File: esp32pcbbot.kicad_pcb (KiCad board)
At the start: 2 copper layers, 110 x 170 mm, 44 parts, among them IC1 BMI055, J1 TB002-500-02BE, J2 TB002-500-02BE, J3 TB002-500-02BE, J4 215299-4, J5 SSQ-120-01-L-D, J6 215299-4, Q1 2N7002, Q2 2N7002, Q3 Q_Photo_NPN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

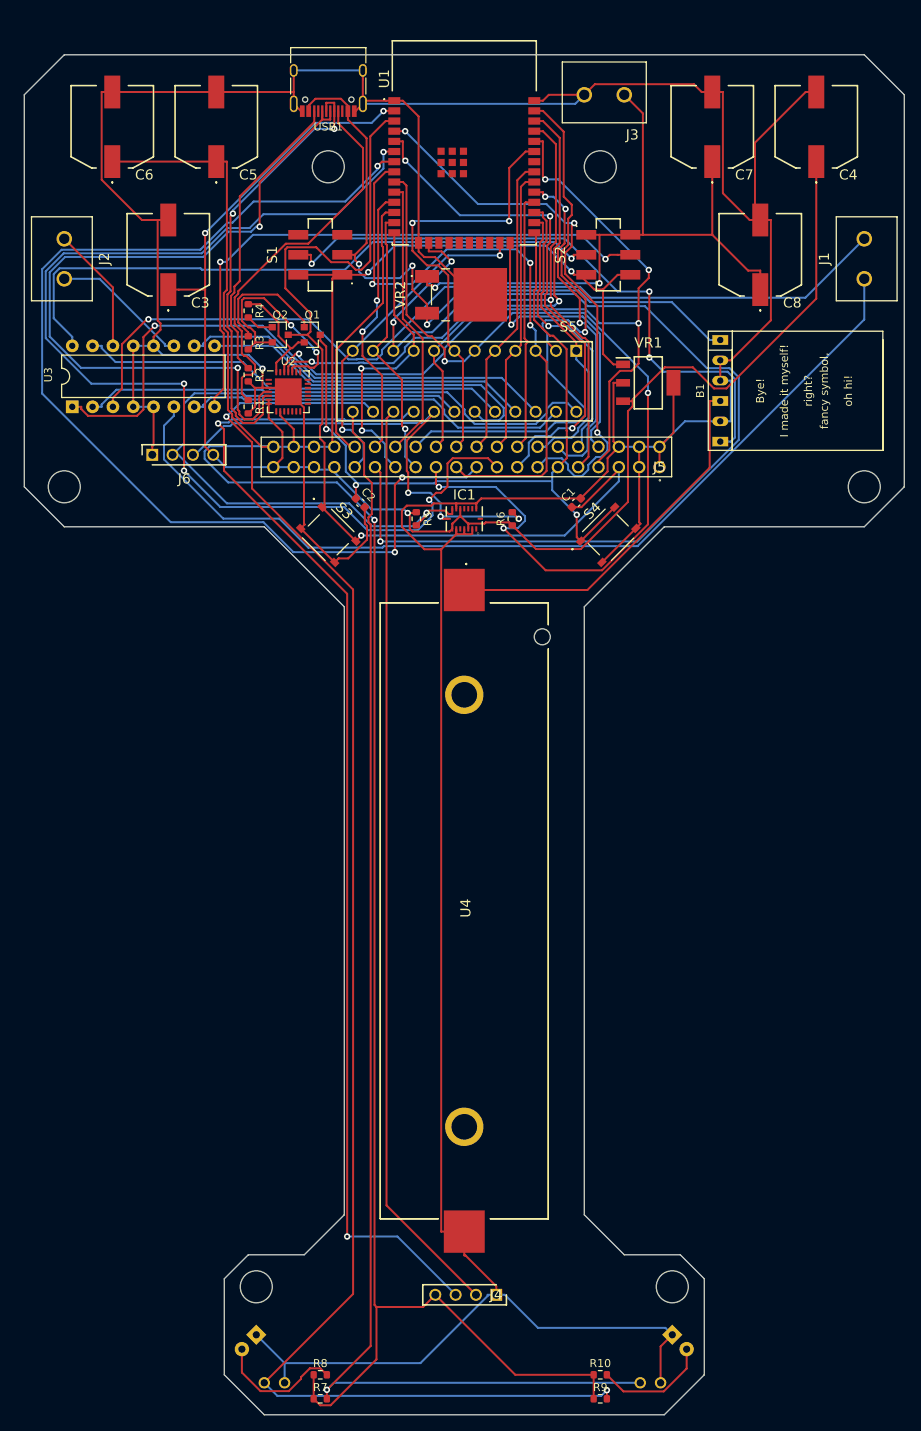
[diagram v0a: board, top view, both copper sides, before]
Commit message: Rearranged and added new spectra DSN
Hoping for better results and better luck with higher power traces for motors and power lines
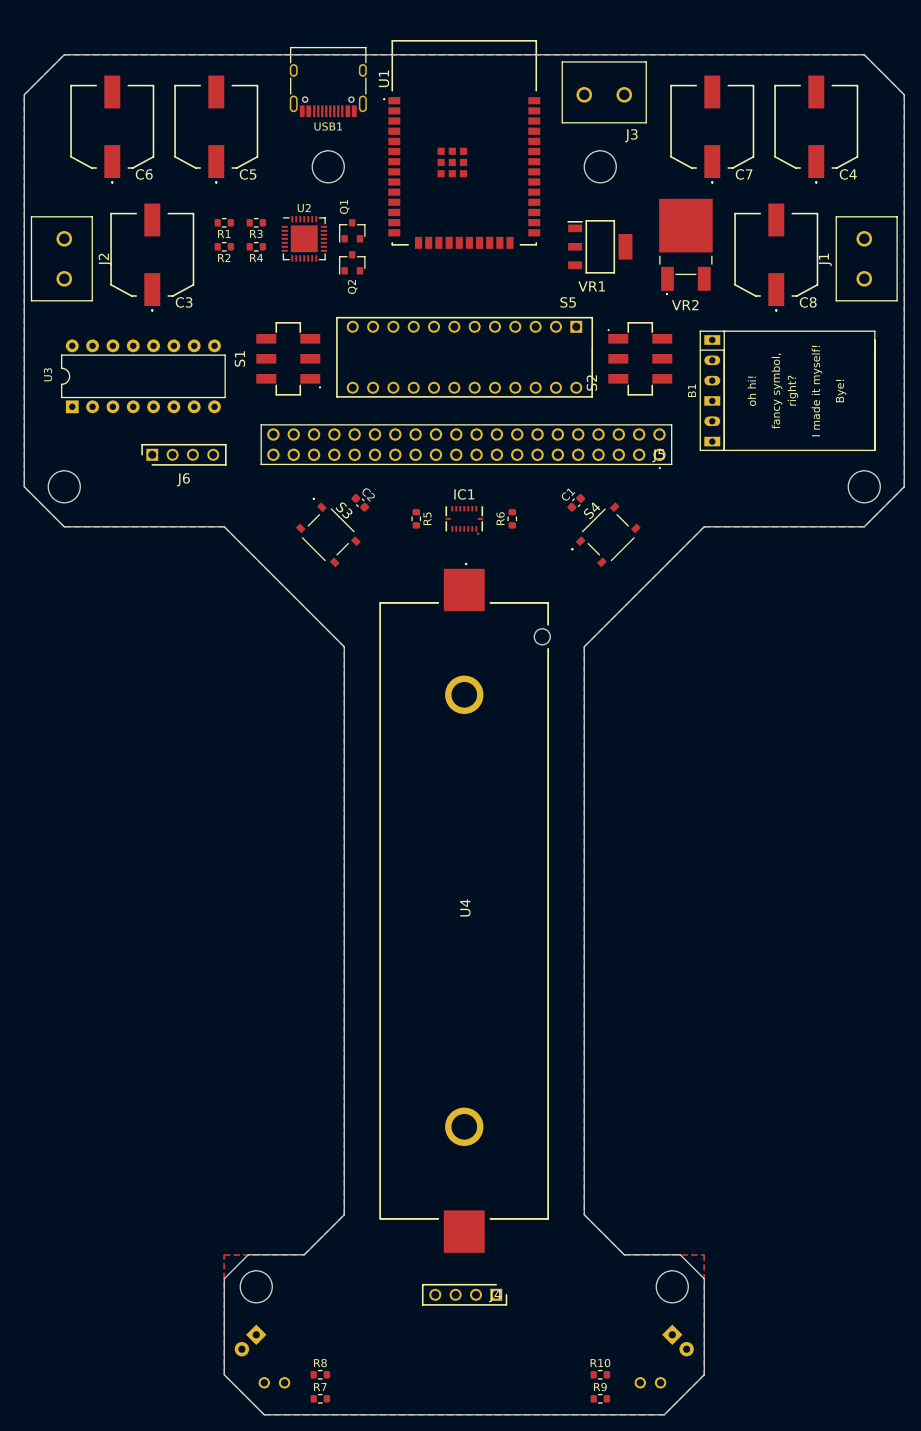
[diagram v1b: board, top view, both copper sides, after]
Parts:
- moved VR2 29.5 mm to (117.7, 49.7), turned to 0 degrees
- moved R1 23.2 mm to (60.0, 46.0), turned to 180 degrees
- moved U2 19.2 mm to (70.0, 48.0)
- moved VR1 18.0 mm to (107.0, 49.0)
- moved R2 16.3 mm to (60.0, 49.0), turned to 180 degrees
- moved R3 15.0 mm to (64.0, 46.0), turned to 180 degrees
- moved Q1 13.9 mm to (76.0, 47.0), turned to 90 degrees
- moved S1 13.6 mm to (68.0, 63.0)
- moved S2 13.6 mm to (112.0, 63.0)
- moved Q2 12.7 mm to (76.0, 51.0), turned to 90 degrees
- moved R4 8.06 mm to (64.0, 49.0), turned to 180 degrees
- moved S5 3.00 mm to (104.0, 59.0)
- moved C3 2.00 mm to (51.0, 50.0)
- moved C8 2.00 mm to (129.0, 50.0)
- moved J5 1.54 mm to (114.4, 75.0)
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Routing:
- net GND: track 583.7 -> 0.00 mm, vias 1 -> 0
- net +5V: track 333.9 -> 0.00 mm, vias 3 -> 0
- net +3V3: track 199.4 -> 0.00 mm, vias 3 -> 0
- net 11Y: track 196.3 -> 0.00 mm, vias 2 -> 0
- net 12Y: track 166.5 -> 0.00 mm, vias 1 -> 0
- net 9Y: track 150.1 -> 0.00 mm, vias 2 -> 0
- net Net-(J5-Pad17): track 139.7 -> 0.00 mm, vias 4 -> 0
- net Net-(J5-Pad19): track 137.2 -> 0.00 mm, vias 3 -> 0
- net 10A: track 136.5 -> 0.00 mm, vias 3 -> 0
- net EN: track 121.2 -> 0.00 mm, vias 1 -> 0
- net Net-(J5-Pad23): track 116.8 -> 0.00 mm, vias 4 -> 0
- net M1B: track 116.1 -> 0.00 mm
- net 10Y: track 115.4 -> 0.00 mm
- net M1A: track 112.2 -> 0.00 mm, vias 1 -> 0
- net Net-(J5-Pad7): track 103.1 -> 0.00 mm, vias 4 -> 0
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- added copper zone on B.Cu, net GND
- added copper zone on F.Cu, net GND
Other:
- outline, holes or cut-outs redrawn

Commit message: re updated DSN for autorouting
i did a dumb and fogot to add the actual motor pins
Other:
- net class Power added: clearance 0.2, trace_width 0.4, via_dia 1, via_drill 0.5
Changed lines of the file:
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@@
     (uvia_dia 0.3)
     (uvia_drill 0.1)
-    (add_net +3V3)
-    (add_net +5V)
-    (add_net +BATT)
     (add_net 10A)
     (add_net 10Y)
@@
     (add_net EN)
     (add_net GND)
-    (add_net M1A)
-    (add_net M1B)
-    (add_net M2A)
-    (add_net M2B)
     (add_net "Net-(B1-Pad4)")
     (add_net "Net-(D1-Pad2)")
@@
     (add_net "Net-(USB1-PadA8)")
     (add_net "Net-(USB1-PadB8)")
+  )
+  (net_class Power ""
+    (clearance 0.2)
+    (trace_width 0.4)
+    (via_dia 1)
+    (via_drill 0.5)
+    (uvia_dia 0.3)
+    (uvia_drill 0.1)
+    (add_net +3V3)
+    (add_net +5V)
+    (add_net +BATT)
+    (add_net M1A)
+    (add_net M1B)
+    (add_net M2A)
+    (add_net M2B)
     (add_net VBUS)
     (add_net VCC)
@@
     (fp_line (start -50.985 2.75) (end -50.985 -4.945) (layer F.CrtYd) (width 0.05))
     (fp_circle (center 0.05 1.65) (end 0.05 1.7) (layer F.SilkS) (width 0.2))
-    (fp_text user %R (at 0 0) (layer F.Fab)
+    (fp_text user %R (at 3.6 2) (layer F.Fab)
       (effects (font (size 1.27 1.27) (thickness 0.254)))
     )
@@
     (descr TB002-500-02BE-1)
     (tags Connector)
-    (fp_text reference J2 (at 2.5 5 90) (layer F.SilkS)
+    (fp_text reference J2 (at -6 -3 90) (layer F.SilkS)
       (effects (font (size 1.27 1.27) (thickness 0.254)))
     )
@@
     (descr TB002-500-02BE-1)
     (tags Connector)
-    (fp_text reference J1 (at 2.5 5 90) (layer F.SilkS)
-      (effects (font (size 1.27 1.27) (thickness 0.254)))
-    )
+    (fp_text reference J1 (at 10 -3 90) (layer F.SilkS)
+      (effects (font (size 1.27 1.27) (thickness 0.254)))
+    )

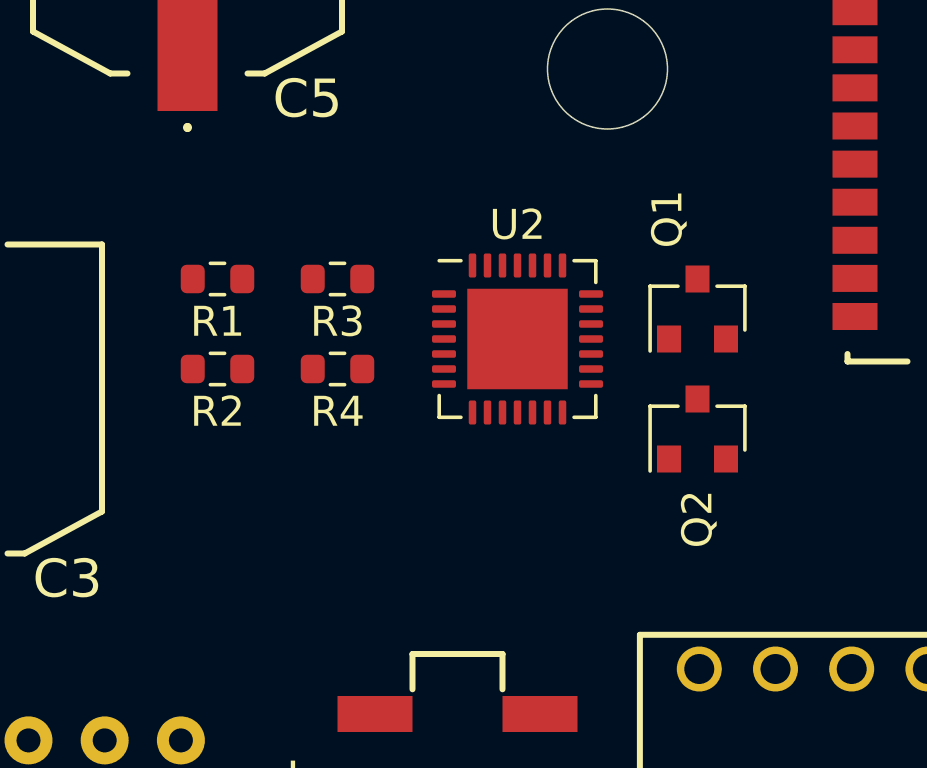
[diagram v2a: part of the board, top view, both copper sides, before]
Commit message: moved CP2102
auto rout was glitching so I moved this to make routing easier
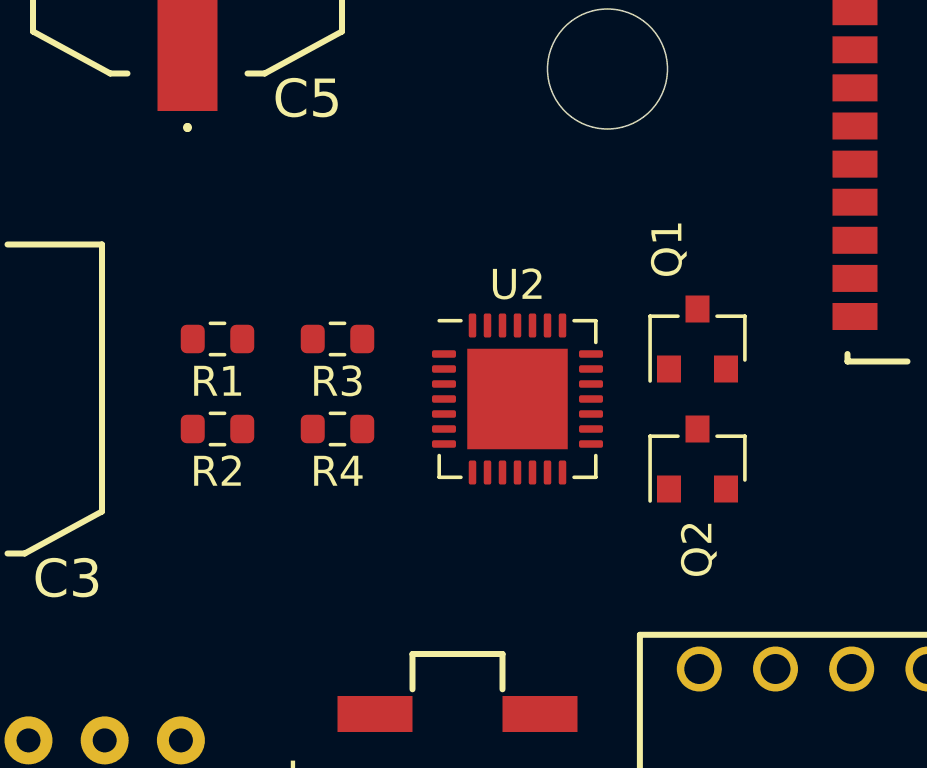
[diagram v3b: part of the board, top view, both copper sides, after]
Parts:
- moved R1 2.00 mm to (60.0, 48.0)
- moved R2 2.00 mm to (60.0, 51.0)
- moved R3 2.00 mm to (64.0, 48.0)
- moved R4 2.00 mm to (64.0, 51.0)
- moved U2 2.00 mm to (70.0, 50.0)
- moved Q1 1.00 mm to (76.0, 48.0)
- moved Q2 1.00 mm to (76.0, 52.0)
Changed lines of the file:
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@@
   )
   (module Package_DFN_QFN:QFN-28-1EP_5x5mm_P0.5mm_EP3.35x3.35mm (layer F.Cu)
-    (at 70 48)
+    (at 70 50)
     (descr "QFN, 28 Pin (http://ww1.microchip.com/downloads/en/PackagingSpec/00000049BQ.pdf#page=283), generated with kicad-footprint-generator ipc_noLead_generator.py")
     (tags "QFN NoLead")
@@
   )
   (module Resistor_SMD:R_0603_1608Metric (layer F.Cu)
-    (at 64 49 180)
+    (at 64 51 180)
     (descr "Resistor SMD 0603 (1608 Metric), square (rectangular) end terminal, IPC_7351 nominal, (Body size source: IPC-SM-782 page 72, https://www.pcb-3d.com/wordpress/wp-content/uploads/ipc-sm-782a_amendment_1_and_2.pdf), generated with kicad-footprint-generator")
     (tags resistor)
@@
   )
   (module Resistor_SMD:R_0603_1608Metric (layer F.Cu)
-    (at 64 46 180)
+    (at 64 48 180)
     (descr "Resistor SMD 0603 (1608 Metric), square (rectangular) end terminal, IPC_7351 nominal, (Body size source: IPC-SM-782 page 72, https://www.pcb-3d.com/wordpress/wp-content/uploads/ipc-sm-782a_amendment_1_and_2.pdf), generated with kicad-footprint-generator")
     (tags resistor)
@@
   )
   (module Resistor_SMD:R_0603_1608Metric (layer F.Cu)
-    (at 60 49 180)
+    (at 60 51 180)
     (descr "Resistor SMD 0603 (1608 Metric), square (rectangular) end terminal, IPC_7351 nominal, (Body size source: IPC-SM-782 page 72, https://www.pcb-3d.com/wordpress/wp-content/uploads/ipc-sm-782a_amendment_1_and_2.pdf), generated with kicad-footprint-generator")
     (tags resistor)
@@
   )
   (module Resistor_SMD:R_0603_1608Metric (layer F.Cu)
-    (at 60 46 180)
+    (at 60 48 180)
     (descr "Resistor SMD 0603 (1608 Metric), square (rectangular) end terminal, IPC_7351 nominal, (Body size source: IPC-SM-782 page 72, https://www.pcb-3d.com/wordpress/wp-content/uploads/ipc-sm-782a_amendment_1_and_2.pdf), generated with kicad-footprint-generator")
     (tags resistor)
@@
   )
   (module Package_TO_SOT_SMD:SOT-23 (layer F.Cu)
-    (at 76 51 90)
+    (at 76 52 90)
     (descr "SOT-23, Standard")
     (tags SOT-23)
@@
   )
   (module Package_TO_SOT_SMD:SOT-23 (layer F.Cu)
-    (at 76 47 90)
+    (at 76 48 90)
     (descr "SOT-23, Standard")
     (tags SOT-23)
